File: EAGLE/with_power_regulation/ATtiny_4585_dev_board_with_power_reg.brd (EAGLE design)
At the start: 43.4 x 59.6 mm, 19 parts, among them IC3 7805, J1 AVR_SPI_PRG_62X3_LOCK

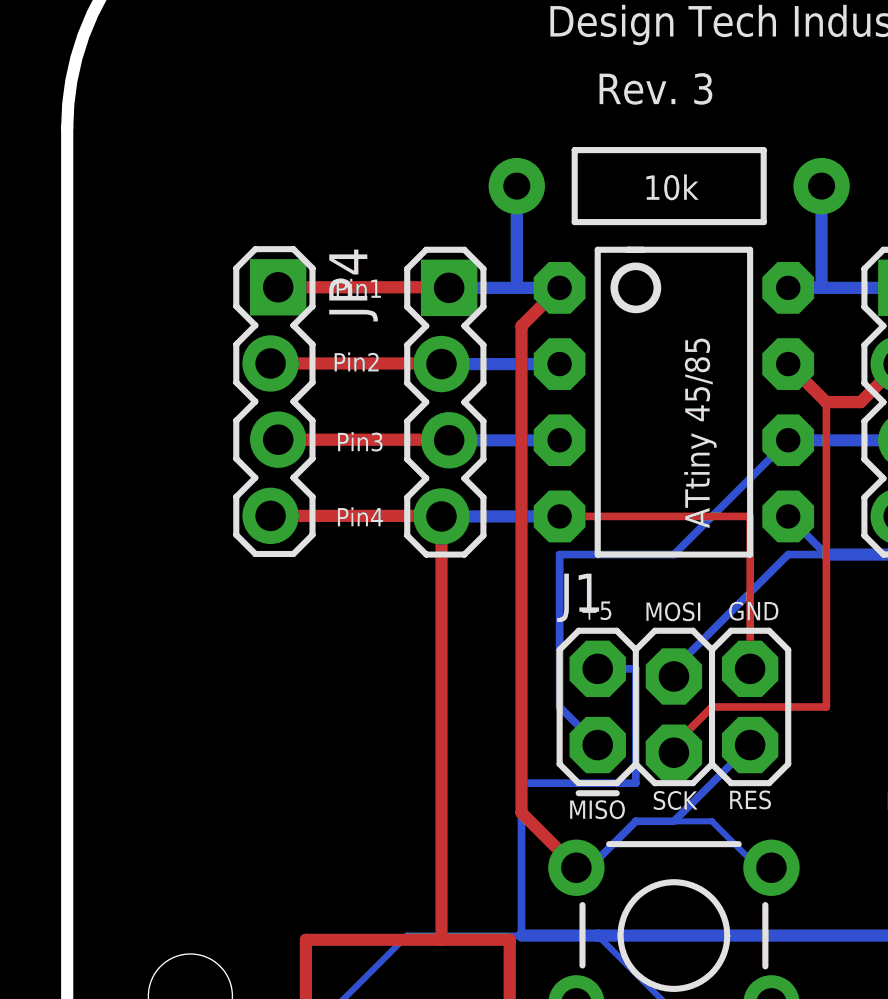
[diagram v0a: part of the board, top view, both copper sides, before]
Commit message: Update of design files. Minor changes to thermocouple solder pads. New board images in 'docs' folder.
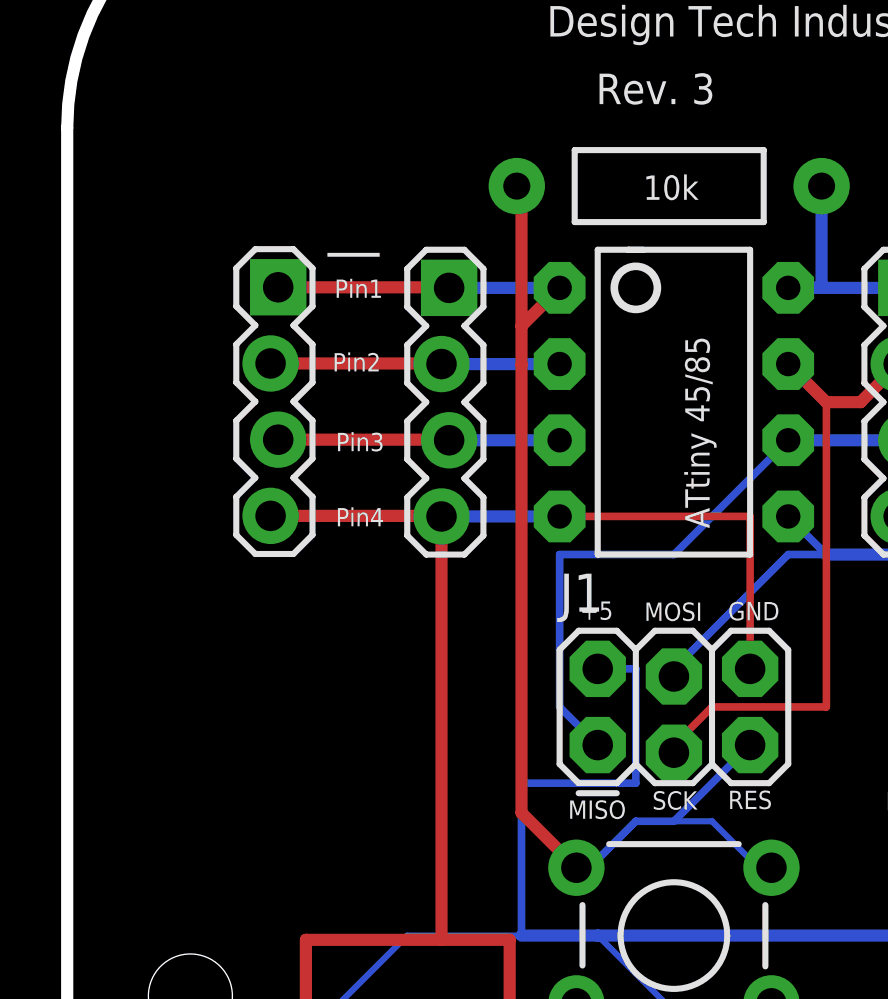
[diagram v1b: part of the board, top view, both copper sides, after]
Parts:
- removed U$2: CREATIVE_COMMONS, SparkFun-Aesthetics:CREATIVE_COMMONS
- renumbered JP4 to |
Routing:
- net N$3: track 44.7 -> 46.1 mm
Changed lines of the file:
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@@
 <element name="U$3" library="SparkFun-Aesthetics" package="OSHW-LOGO-M" value="OSHW-LOGOM" x="55.408371875" y="27.33639375"/>
 <element name="JP3" library="SparkFun" package="1X04_LOCK" value="" x="59.0414875" y="44.418403125" rot="R270"/>
-<element name="JP4" library="SparkFun" package="1X04_LOCK" value="" x="32.402275" y="44.4697125" rot="R270"/>
-<element name="U$2" library="SparkFun-Aesthetics" package="CREATIVE_COMMONS" value="CREATIVE_COMMONS" x="46.168359375" y="-9.08801875"/>
+<element name="|" library="SparkFun" package="1X04_LOCK" value="" x="32.402275" y="44.4697125" rot="R270"/>
 </elements>
 <signals>
@@
 <wire x1="40.2463" y1="20.313803125" x2="42.92245625" y2="20.313803125" width="0.4064" layer="1"/>
 <wire x1="42.92245625" y1="20.313803125" x2="42.92245625" y2="20.421178125" width="0.4064" layer="1"/>
-<contactref element="JP4" pad="4"/>
+<contactref element="|" pad="4"/>
 <wire x1="32.275275" y1="36.8497125" x2="37.973" y2="36.8497125" width="0.4064" layer="1"/>
 <wire x1="37.973" y1="36.8497125" x2="37.973" y2="36.83" width="0.4064" layer="1"/>
@@
 <wire x1="45.72" y1="26.67" x2="48.26" y2="29.21" width="0.254" layer="16"/>
 <wire x1="42.4688" y1="25.1206" x2="43.18" y2="25.4" width="0.254" layer="16"/>
-<wire x1="41.91" y1="44.45" x2="40.482215625" y2="44.45" width="0.4064" layer="16"/>
-<wire x1="40.482215625" y1="44.45" x2="38.227" y2="44.45" width="0.4064" layer="16"/>
+<wire x1="41.91" y1="44.45" x2="38.227" y2="44.45" width="0.4064" layer="16"/>
 <wire x1="40.64" y1="43.18" x2="41.91" y2="44.45" width="0.4064" layer="1"/>
-<wire x1="40.64" y1="26.9494" x2="40.64" y2="43.18" width="0.4064" layer="1"/>
+<wire x1="40.64" y1="26.9494" x2="40.64" y2="41.88744375" width="0.4064" layer="1"/>
+<wire x1="40.64" y1="41.88744375" x2="40.64" y2="43.18" width="0.4064" layer="1"/>
 <wire x1="42.4688" y1="25.1206" x2="40.64" y2="26.9494" width="0.4064" layer="1"/>
 <contactref element="R2" pad="P$2"/>
@@
 <wire x1="45.72" y1="26.67" x2="46.99" y2="26.67" width="0.2032" layer="16"/>
 <wire x1="48.26" y1="25.4" x2="48.9712" y2="25.1206" width="0.2032" layer="16"/>
-<wire x1="40.482215625" y1="44.45" x2="40.482215625" y2="47.842321875" width="0.4064" layer="16"/>
-<contactref element="JP4" pad="1"/>
+<contactref element="|" pad="1"/>
 <wire x1="32.529275" y1="44.4697125" x2="38.227" y2="44.4697125" width="0.4064" layer="1"/>
 <wire x1="38.227" y1="44.4697125" x2="38.227" y2="44.45" width="0.4064" layer="1"/>
+<wire x1="40.482215625" y1="47.842321875" x2="40.64" y2="47.842321875" width="0.4064" layer="1"/>
+<wire x1="40.64" y1="47.842321875" x2="40.64" y2="43.18" width="0.4064" layer="1"/>
 </signal>
 <signal name="N$6">
@@
 <contactref element="JP2" pad="2"/>
 <wire x1="37.973" y1="41.91" x2="41.91" y2="41.91" width="0.4064" layer="16"/>
-<contactref element="JP4" pad="2"/>
+<contactref element="|" pad="2"/>
 <wire x1="32.275275" y1="41.9297125" x2="37.973" y2="41.9297125" width="0.4064" layer="1"/>
 <wire x1="37.973" y1="41.9297125" x2="37.973" y2="41.91" width="0.4064" layer="1"/>
@@
 <contactref element="JP2" pad="3"/>
 <wire x1="38.227" y1="39.37" x2="41.91" y2="39.37" width="0.4064" layer="16"/>
-<contactref element="JP4" pad="3"/>
+<contactref element="|" pad="3"/>
 <wire x1="32.529275" y1="39.3897125" x2="38.227" y2="39.3897125" width="0.4064" layer="1"/>
 <wire x1="38.227" y1="39.3897125" x2="38.227" y2="39.37" width="0.4064" layer="1"/>
